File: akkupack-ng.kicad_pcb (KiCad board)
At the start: 4 copper layers, 110 x 80 mm, 135 parts, among them J101 12V OUT, J102 36V IN, J103 36V OUT, J104 BAT, J105 OUT, J106 IN, J107 LED SW, J108 TEMP, J201 DISP, J202 SWD, J203 SPI, J204 USB serial, J301 USB serial, J401 USB serial, Q101 2N7002, Q102 BSS84, Q103 2N7002, Q201 2N7002, SW101 LED Enable, SW201 Reset, U101 BQ34Z100PWR-G1, U102 74HC164, U103 74HC164, U201 STM32F103CBT6, U202 USBLC6-2SC6, U203 AMS1117-3.3, U301 USBLC6-2SC6, U302 XC6206PxxxMR, U303 CH330N, U401 USBLC6-2SC6, U402 XC6206PxxxMR, U403 CH330N, Y201 8MHz, Y202 32k

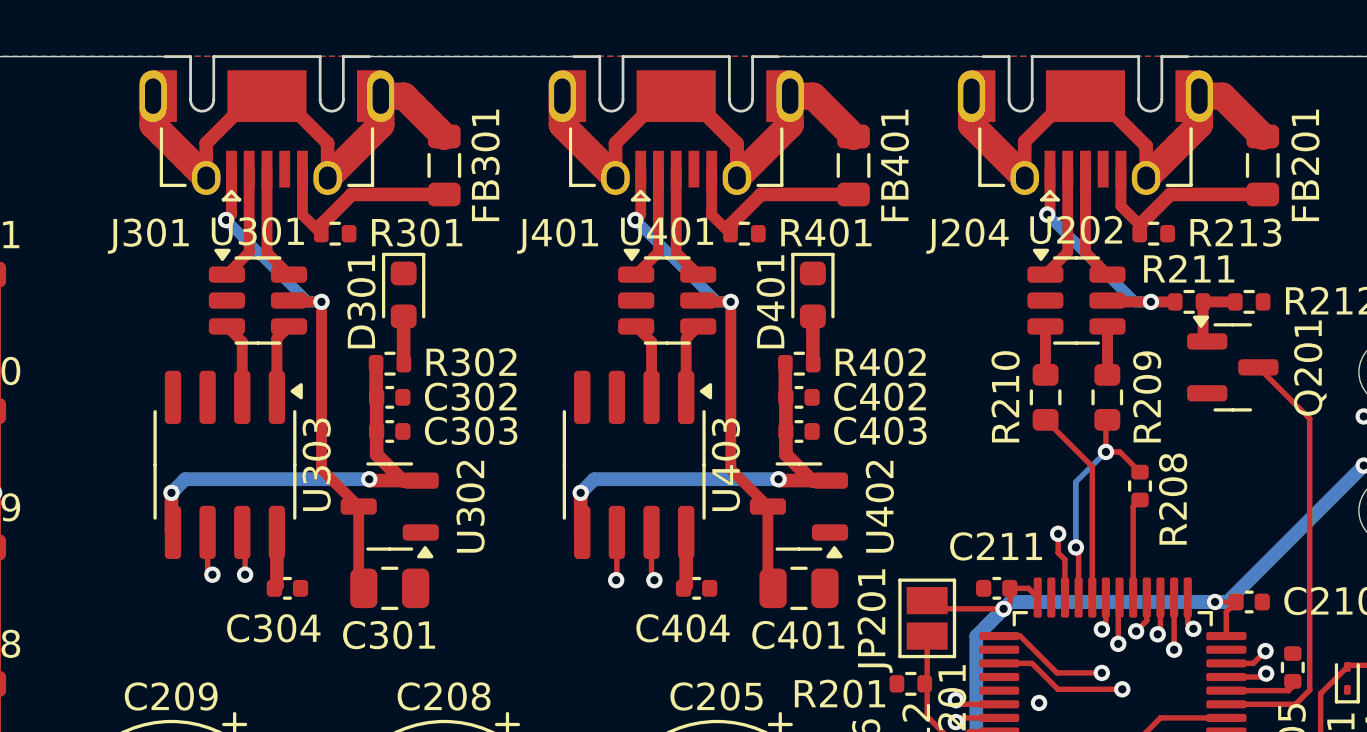
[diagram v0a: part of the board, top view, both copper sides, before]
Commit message: Fix USB
Signed-off-by: Benedikt Spranger <b.spranger@linutronix.de>
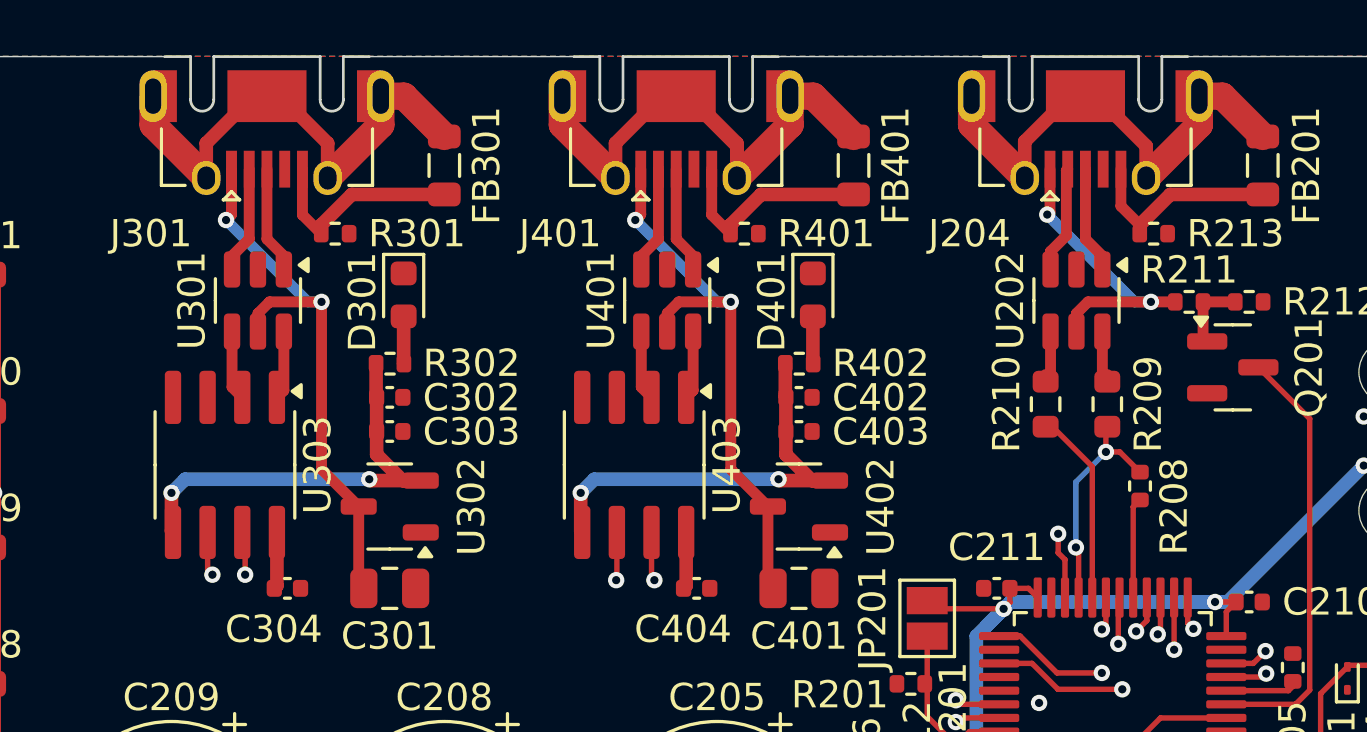
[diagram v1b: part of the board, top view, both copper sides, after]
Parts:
- moved R209 0.25 mm to (140.8, 57.8)
- moved R210 0.25 mm to (138.5, 57.8)
- turned U202 to -90 degrees
- turned U301 to -90 degrees
- turned U401 to -90 degrees
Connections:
- U202 pad 1: Net-(J204-D-) -> Net-(J204-D+)
- U202 pad 3: Net-(R210-Pad2) -> Net-(J204-D-)
- U202 pad 4: Net-(R209-Pad2) -> Net-(R210-Pad2)
- U202 pad 6: Net-(J204-D+) -> Net-(R209-Pad2)
- U301 pad 1: /MCU/serial1/D- -> /MCU/serial1/D+
- U301 pad 3: /MCU/serial1/UD- -> /MCU/serial1/D-
- U301 pad 4: /MCU/serial1/UD+ -> /MCU/serial1/UD-
- U301 pad 6: /MCU/serial1/D+ -> /MCU/serial1/UD+
- U401 pad 1: /MCU/serial2/D- -> /MCU/serial2/D+
- U401 pad 3: /MCU/serial2/UD- -> /MCU/serial2/D-
- U401 pad 4: /MCU/serial2/UD+ -> /MCU/serial2/UD-
- U401 pad 6: /MCU/serial2/D+ -> /MCU/serial2/UD+
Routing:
- net Net-(J204-VBUS): track 9.34 -> 11.3 mm
- net Net-(J301-VBUS): track 19.0 -> 21.0 mm
- net Net-(J401-VBUS): track 19.0 -> 21.0 mm

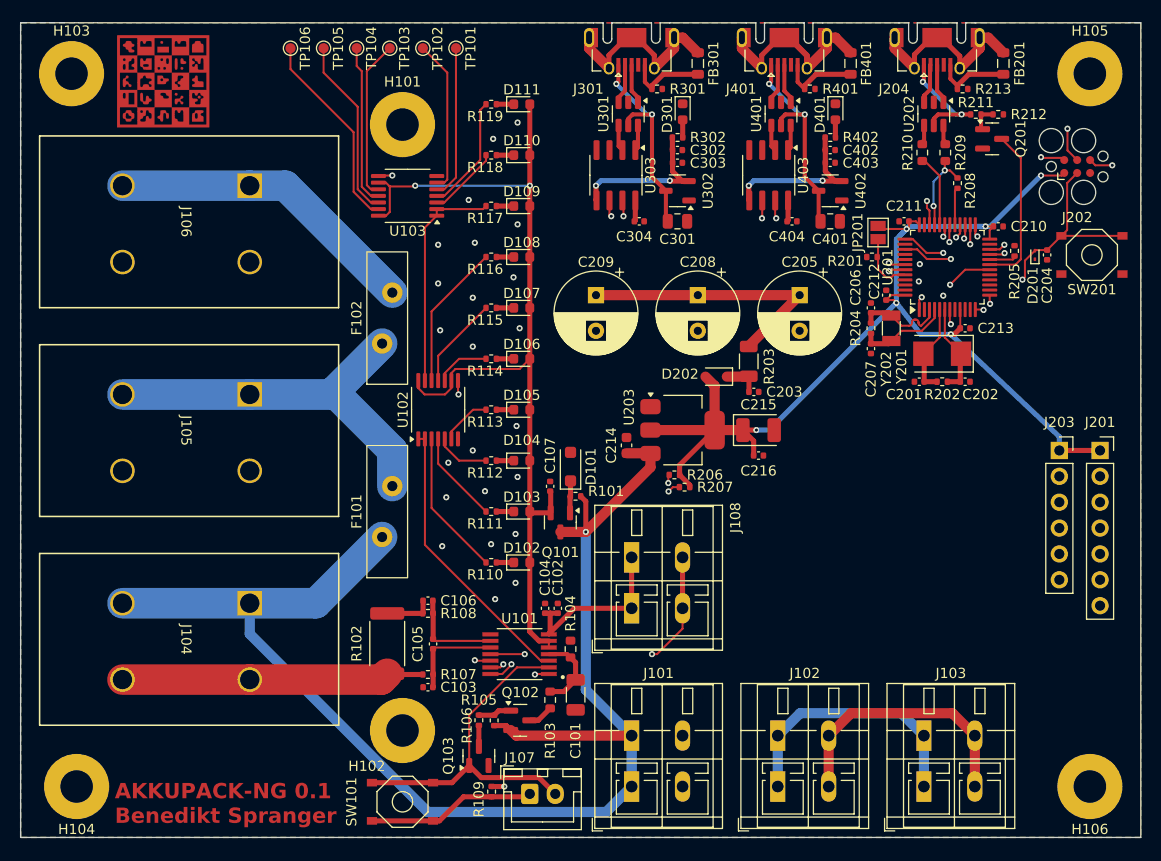
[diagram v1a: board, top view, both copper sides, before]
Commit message: Update to KiCAD 9.x
Signed-off-by: Benedikt Spranger <b.spranger@linutronix.de>
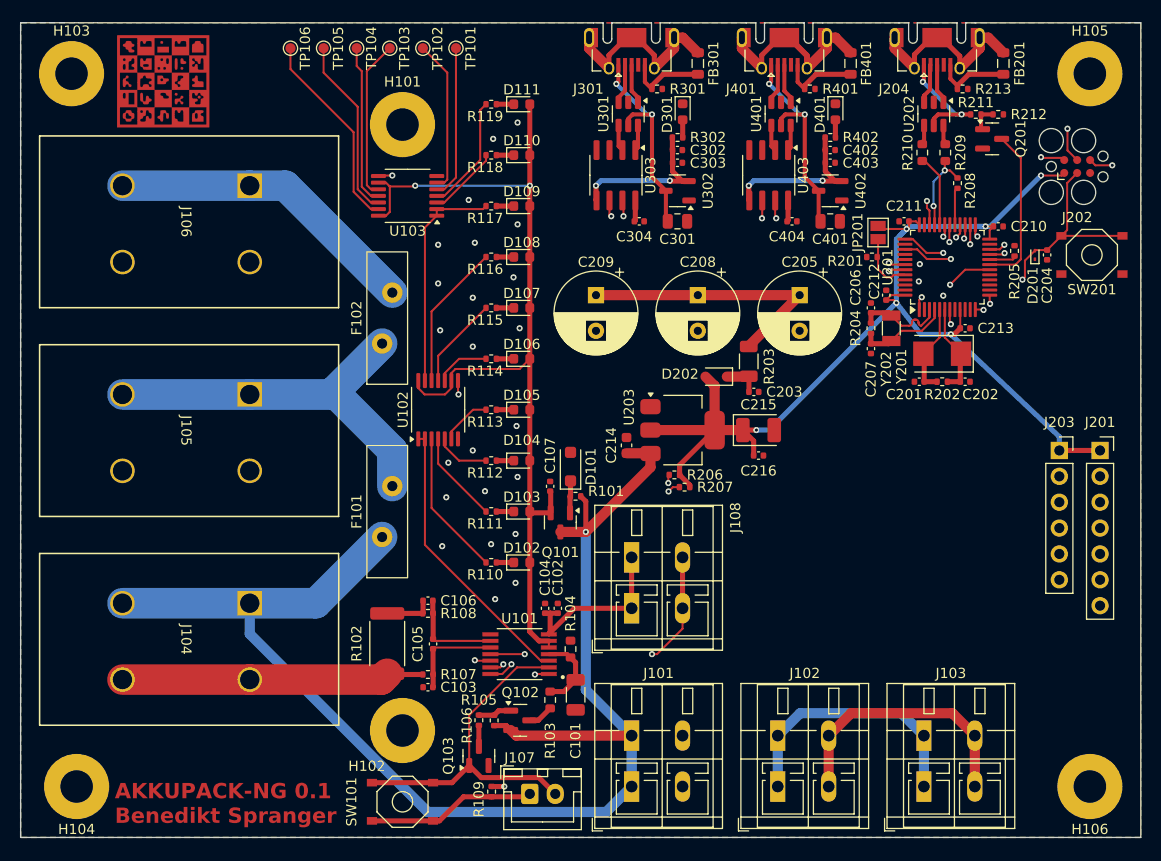
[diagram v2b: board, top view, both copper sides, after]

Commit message: Rework Input selection
Signed-off-by: Benedikt Spranger <b.spranger@linutronix.de>
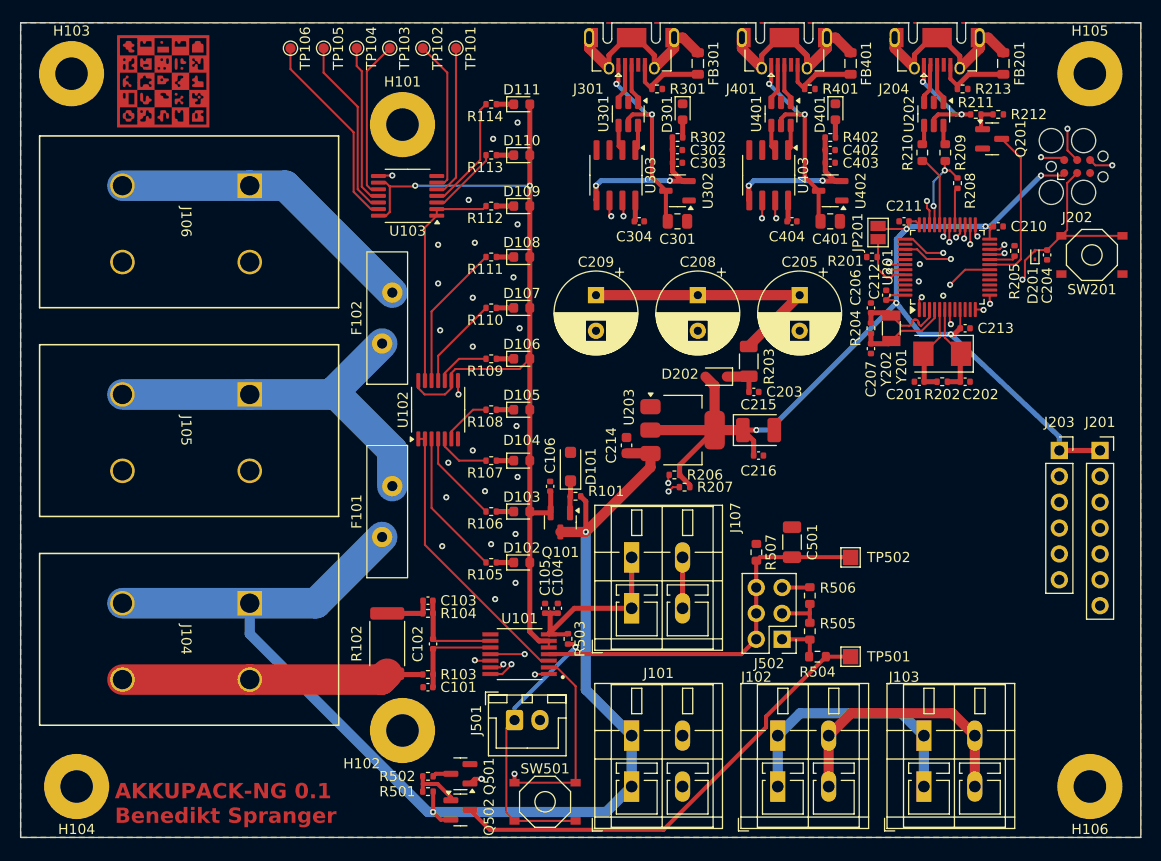
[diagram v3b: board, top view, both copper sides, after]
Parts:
- removed the C101 at (104.5, 111.0)
- removed the J107 at (100.0, 120.7)
- removed Q102: BSS84, Package_TO_SOT_SMD:SOT-23
- removed Q103: 2N7002, Package_TO_SOT_SMD:SOT-23
- removed the R103 at (102.0, 111.5)
- removed the R104 at (104.0, 106.5)
- removed the R105 at (96.5, 113.5)
- removed the R106 at (95.0, 113.5)
- removed the R109 at (96.2, 120.5)
- removed SW101: LED Enable, footprint:Push_SW_5x5
- added C501: 3300p, Capacitor_SMD:C_1206_3216Metric, F.Cu at (125.8, 96.0)
- added J501: LED SW, Connector_JST:JST_XH_B2B-XH-A_1x02_P2.50mm_Vertical, F.Cu at (98.5, 113.5)
- added J502: Voltage sel, Connector_PinHeader_2.54mm:PinHeader_2x03_P2.54mm_Vertical, F.Cu at (124.8, 105.5)
- added Q501: 2N7002, Package_TO_SOT_SMD:SOT-23, F.Cu at (93.2, 118.8)
- added Q502: BSS84, Package_TO_SOT_SMD:SOT-23, F.Cu at (93.2, 122.3)
- added R501: 100k, Resistor_SMD:R_0402_1005Metric, F.Cu at (90.0, 120.5)
- added R502: 165k, Resistor_SMD:R_0402_1005Metric, F.Cu at (90.0, 119.0)
- added R503: 1k, Resistor_SMD:R_0402_1005Metric, F.Cu at (103.8, 105.5)
- added R504: 300k .1%, Resistor_SMD:R_0603_1608Metric, F.Cu at (128.2, 107.2)
- added R505: 300k .1%, Resistor_SMD:R_0603_1608Metric, F.Cu at (127.5, 104.8)
- added R506: 300k .1%, Resistor_SMD:R_0603_1608Metric, F.Cu at (127.5, 101.2)
- added R507: 16k5 .1%, Resistor_SMD:R_0603_1608Metric, F.Cu at (122.2, 97.0)
- added SW501: LED Enable, footprint:Push_SW_5x5, F.Cu at (101.5, 121.5)
- added TP501: Vscale Hi, TestPoint:TestPoint_Pad_1.5x1.5mm, F.Cu at (131.5, 107.2)
- added TP502: Vscale Lo, TestPoint:TestPoint_Pad_1.5x1.5mm, F.Cu at (131.5, 97.5)
- renumbered C103 to C101, C105 to C102, C106 to C103, C102 to C104, C104 to C105, C107 to C106, J108 to J107, R107 to R103, R108 to R104, R110 to R105, R111 to R106, R112 to R107, R113 to R108, R114 to R109, R115 to R110, R116 to R111, R117 to R112, R118 to R113, R119 to R114
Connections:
- U101 pad 2: Net-(J107-Pin_2) (its old number) -> /Input Selection/Ven
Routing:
- net Net-(Q502-D): track 0.00 -> 45.8 mm
- net Net-(J107-Pin_2) (its old number): track 34.6 -> 0.00 mm
- net /Input Selection/Ven: track 0.00 -> 31.0 mm, vias 0 -> 2
- net /BAT: track 7.65 -> 38.1 mm
- net Net-(J501-Pin_1): track 0.00 -> 27.1 mm, vias 0 -> 1
- net +2V5: track 41.5 -> 19.4 mm, vias 1 -> 0
- net Net-(J107-Pin_1): track 16.6 -> 0.00 mm
- net +12V: track 136.7 -> 126.8 mm, vias 1 -> 2
- net Net-(Q502-G): track 0.00 -> 5.10 mm
- net Net-(J502-Pin_3): track 0.00 -> 4.57 mm
- net Net-(J502-Pin_1): track 0.00 -> 4.45 mm
- net Net-(Q102-G): track 3.32 -> 0.00 mm
- net Net-(J502-Pin_5): track 0.00 -> 2.74 mm
- net Net-(Q102-D): track 2.49 -> 0.00 mm
- net Net-(Q103-D): track 2.06 -> 0.00 mm
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
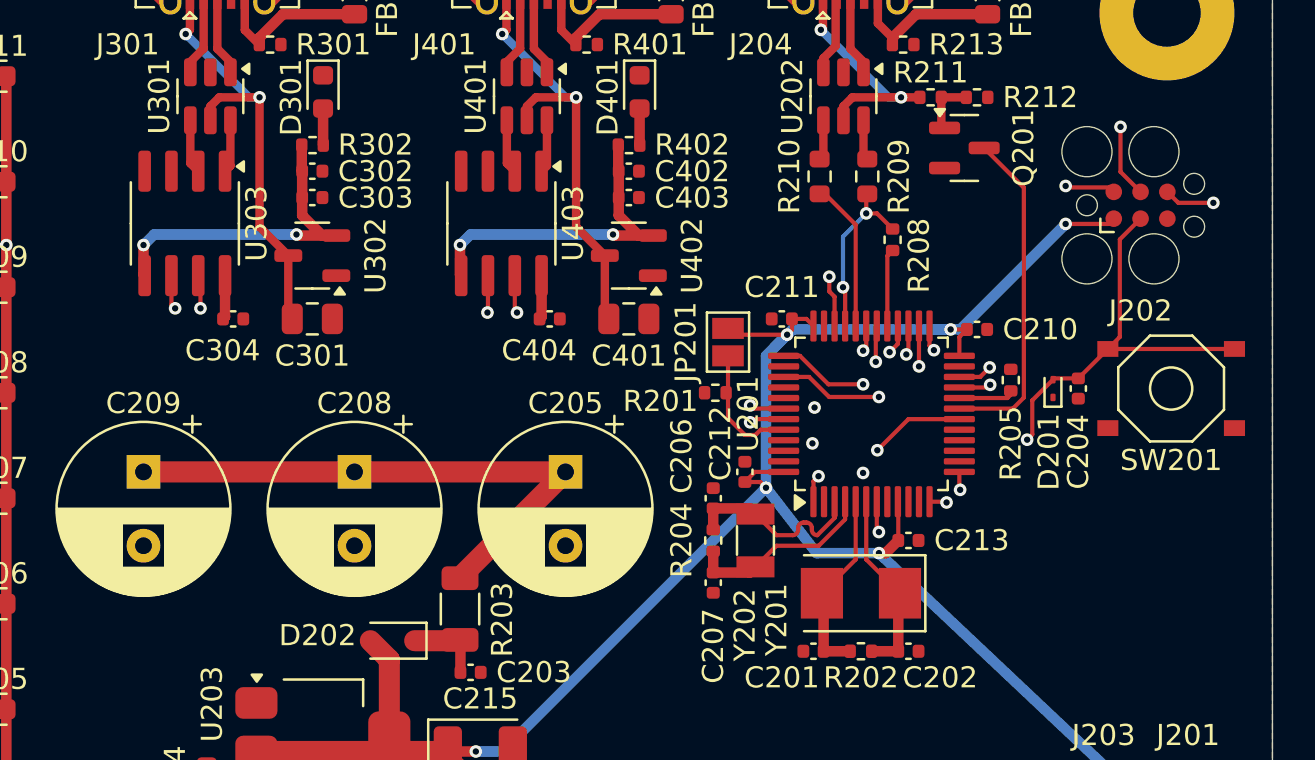
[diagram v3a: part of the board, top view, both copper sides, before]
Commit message: Rework SWD connector
Signed-off-by: Benedikt Spranger <b.spranger@linutronix.de>
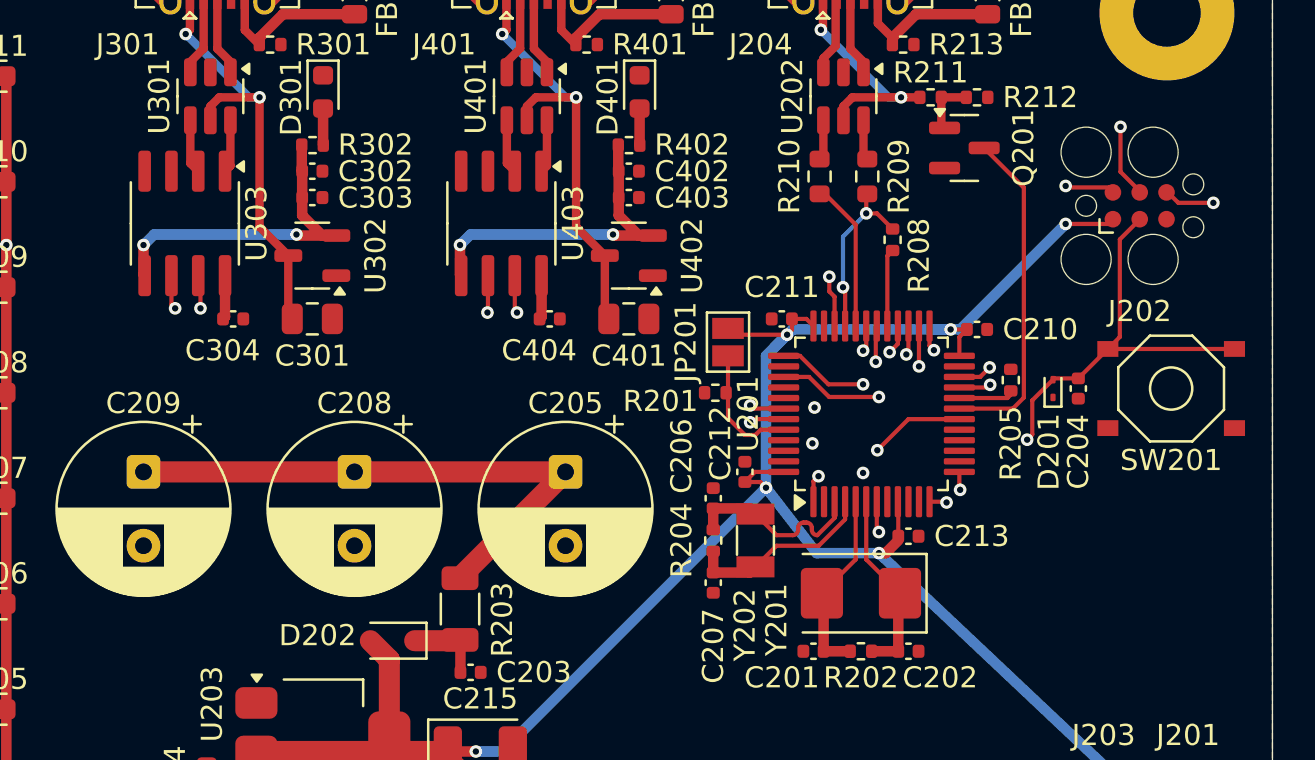
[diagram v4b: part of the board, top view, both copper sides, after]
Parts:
- moved C213 0.20 mm to (142.8, 74.8)
